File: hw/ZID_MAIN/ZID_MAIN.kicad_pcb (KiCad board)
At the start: 2 copper layers, 165.1 x 101.6 mm, 150 parts, among them J1 Conn_01x02_Pin_2.54mm, J10 USB-C PWR ONLY, J11 Conn_01x08, J2 Conn_02x05_2.54mm, J3 Conn_02x05_2.54mm, J4 Conn_02x05_PINHDR_2.54mm, J5 HDR 1x04 Socket, J6 Conn_02x03_Odd_Even, J7 Conn_01x03, J8 BRK-EXP-UNIT, J9 Z80-TARGET, M1 WS-RP2040-Zero, SW1 SW_Push, SW2 SW_DIP_x02, U1 74HCT161, U10 74FCT2245, U11 SST39SF010, U12 AS7C1024B-10J, U13 74FCT541C, U14 74AHCT244, U15 74FCT257T, U16 74HCT166, U17 74HCT166, U18 74LVC245, U19 74LVC125AS, U2 74FCT541C, U20 24LC32, U21 ATF1504AS-44T, U22 74AHCT1G125, U23 74LVC273, U24 74AHCT125, U25 74LVC2G04, U26 74AHCT1G14, U3 74FCT541C, U4 MIC2775, U5 OSC-20MHz, U6 Z80 C20MHz-PLCC, U7 ATF1508AS, U8 74FCT2245, U9 74FCT2245

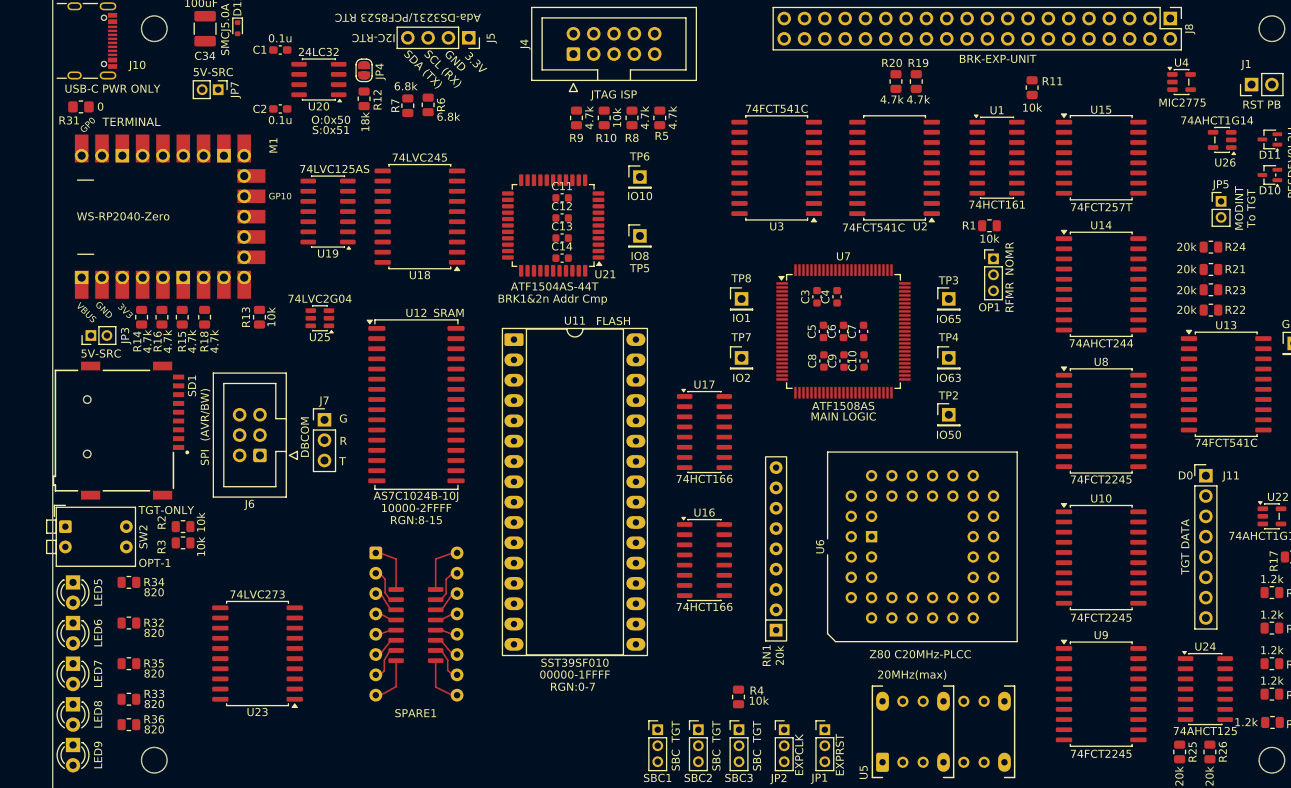
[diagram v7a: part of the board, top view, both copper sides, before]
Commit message: Exp-BP: Add display
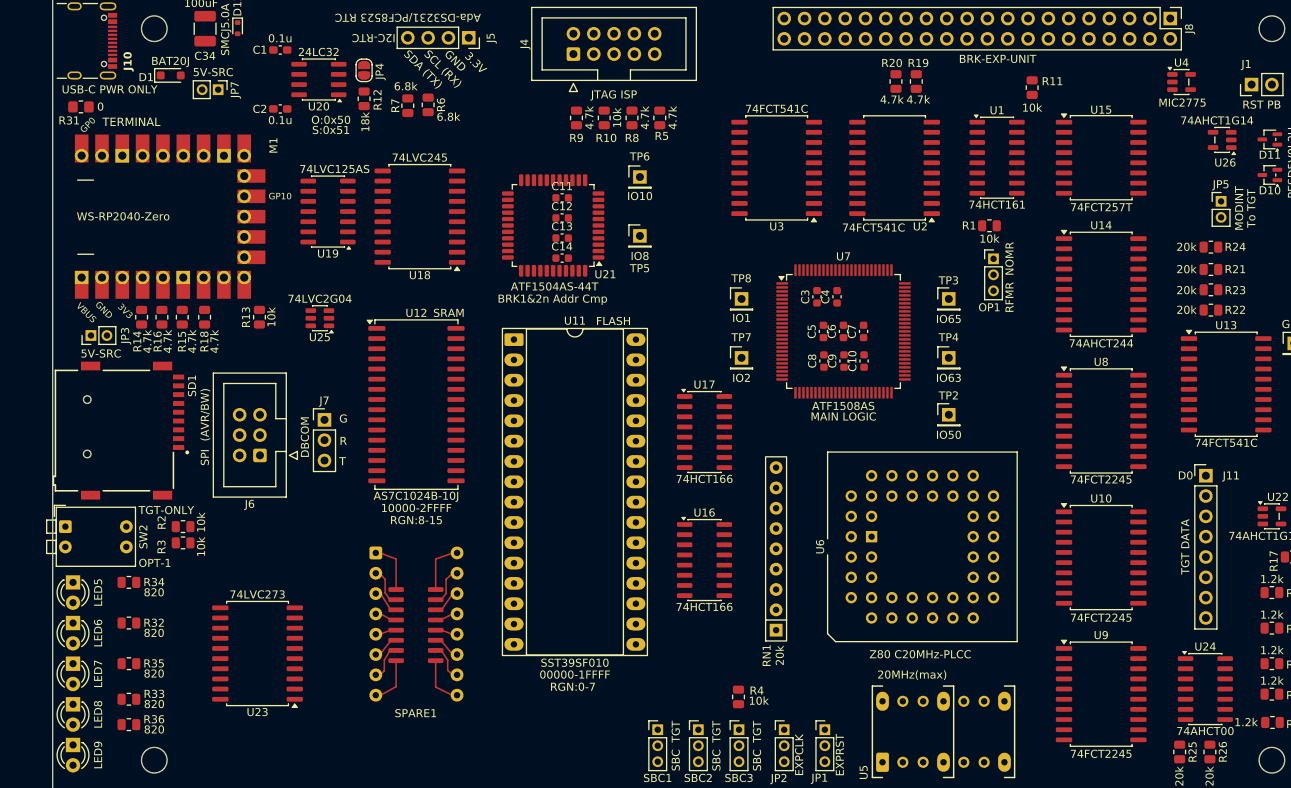
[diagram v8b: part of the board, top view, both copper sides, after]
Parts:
- added D1: BAT20J, Diode_SMD:D_SOD-323_HandSoldering, F.Cu at (86.2, 33.8)
- U24: value 74AHCT125 -> 74AHCT00
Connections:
- JP3 pad 2: +5V -> Net-(D1-K)
- LED10 pad 1: GND -> Net-(LED10-K)
- LED10 pad 2: Net-(LED10-A) -> +5V
- R27 pad 1: Net-(LED1-A) -> Net-(LED1-K)
- R27 pad 2: +5V -> GND
- R28 pad 1: Net-(LED2-A) -> Net-(LED2-K)
- R28 pad 2: +5V -> GND
- R29 pad 1: Net-(LED3-A) -> Net-(LED3-K)
- R29 pad 2: +5V -> GND
- R30 pad 1: Net-(LED4-A) -> Net-(LED4-K)
- R30 pad 2: +5V -> GND
- R37 pad 1: Net-(LED10-A) -> Net-(LED10-K)
- R37 pad 2: +5V -> GND
- U24 pad 1: GND -> TGTMODE-
- U24 pad 10: GND -> TRST-
- U24 pad 11: Net-(LED4-K) -> Net-(LED4-A)
- U24 pad 13: GND -> TRST-
- U24 pad 2: TGTMODE- -> TRST-
- U24 pad 3: Net-(LED1-K) -> Net-(LED1-A)
- U24 pad 4: GND -> ZBACK-
- U24 pad 5: ZBACK- -> TRST-
- U24 pad 6: Net-(LED2-K) -> Net-(LED2-A)
- U24 pad 8: Net-(LED3-K) -> Net-(LED3-A)
